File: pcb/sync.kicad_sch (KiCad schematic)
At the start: 54 parts, among them J1 UP_Out, J2 CLK In, J3 BP_Inv_Out, J4 BP_Out, J5 Power, P1 B100K, P2 B100K, P3 B100K, P4 B100K, SW1 Button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

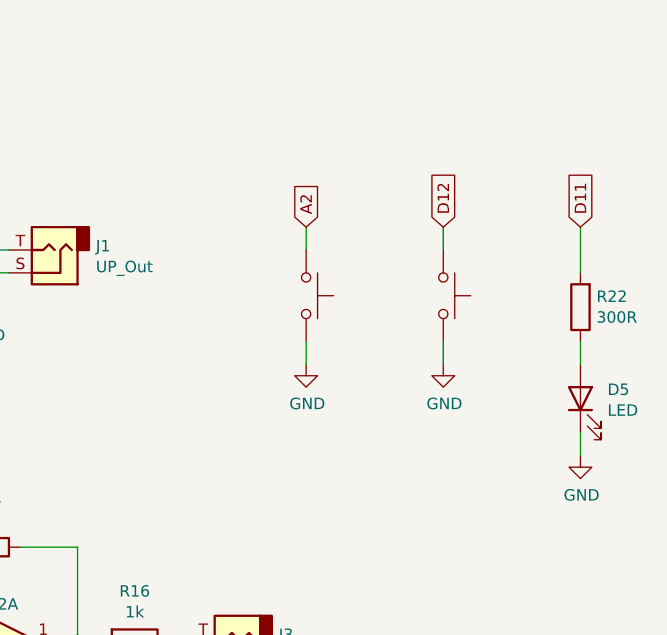
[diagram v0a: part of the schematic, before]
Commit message: Fixed button circuit, updated pcb for smaller footprints,
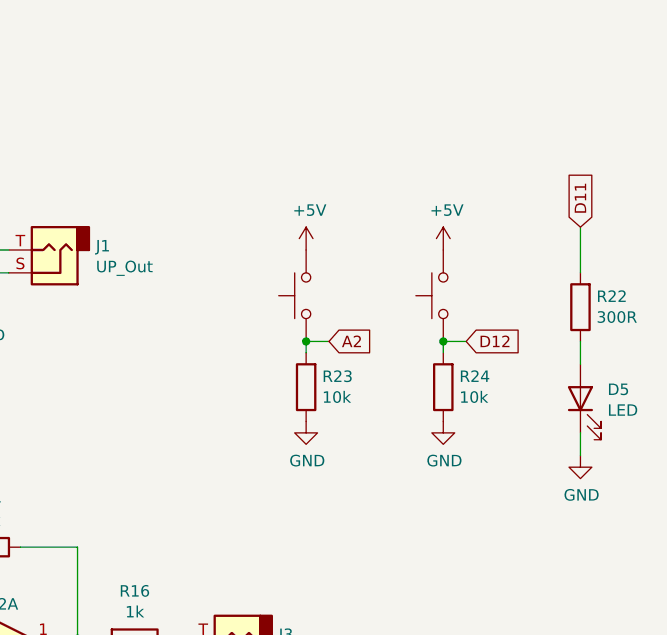
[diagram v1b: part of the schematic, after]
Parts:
- added R23, R24: 10k, Resistor_SMD:R_0402_1005Metric, symbol Device:R
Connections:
- net +5V: now also SW1.2, SW2.2
- net A2: now also R23.2
- net D12: now also R24.2
- net GND: now also R23.1, R24.1; no longer SW1.2, SW2.2
